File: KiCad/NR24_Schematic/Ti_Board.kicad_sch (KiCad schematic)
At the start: 25 parts, among them J5 Dash TI Connection, J5 J1 Pin J3 Pin, J5 J12 (CAN Interface w/ Transce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, J5 J4 Pin J2 Pin, J5 J5 Pin J7 Pin, J5 J8 Pin J6 Pin, J5 XBEE PRO, J6 SpeakON_NL2, J8 CAN Connector, Q1 Q_NMOS_DGS, Q2 Q_NMOS_DGS, Q3 Q_NMOS_DGS

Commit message: NOV1 Changes w Clarks
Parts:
- added J5: J4 Pin J2 Pin, symbol Connector_Generic:Conn_02x06_Counter_Clockwise
- added J5: J1 Pin J3 Pin, symbol Connector_Generic:Conn_02x06_Counter_Clockwise

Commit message: ams with IMD inside
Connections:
- net in_BLK: now also Q1.1 (D), Q2.1 (D); no longer Q1.2 (G), Q2.2 (G)
- net at R3.2: now also Q1.2 (G); no longer Q1.1 (D)
- net Yellow to RCKR Switch: now reaches J5.1 (3.3V)
- net White to CANBUS Plug: now reaches J5.21 (5V)
- net at R4.2: now also Q2.2 (G); no longer Q2.1 (D)
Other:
- moved on the sheet: R3, R4

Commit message: stuff
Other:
- note added: "Old NR23 Dash"
- moved on the sheet: D2, D3, J6, Q1, Q2, Q3, R1, R2, R3, R4

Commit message: AMS with relay
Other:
- note removed: "Old NR23 Dash"
- moved on the sheet: D2, D3, J6, Q1, Q2, Q3, R1, R2, R3, R4

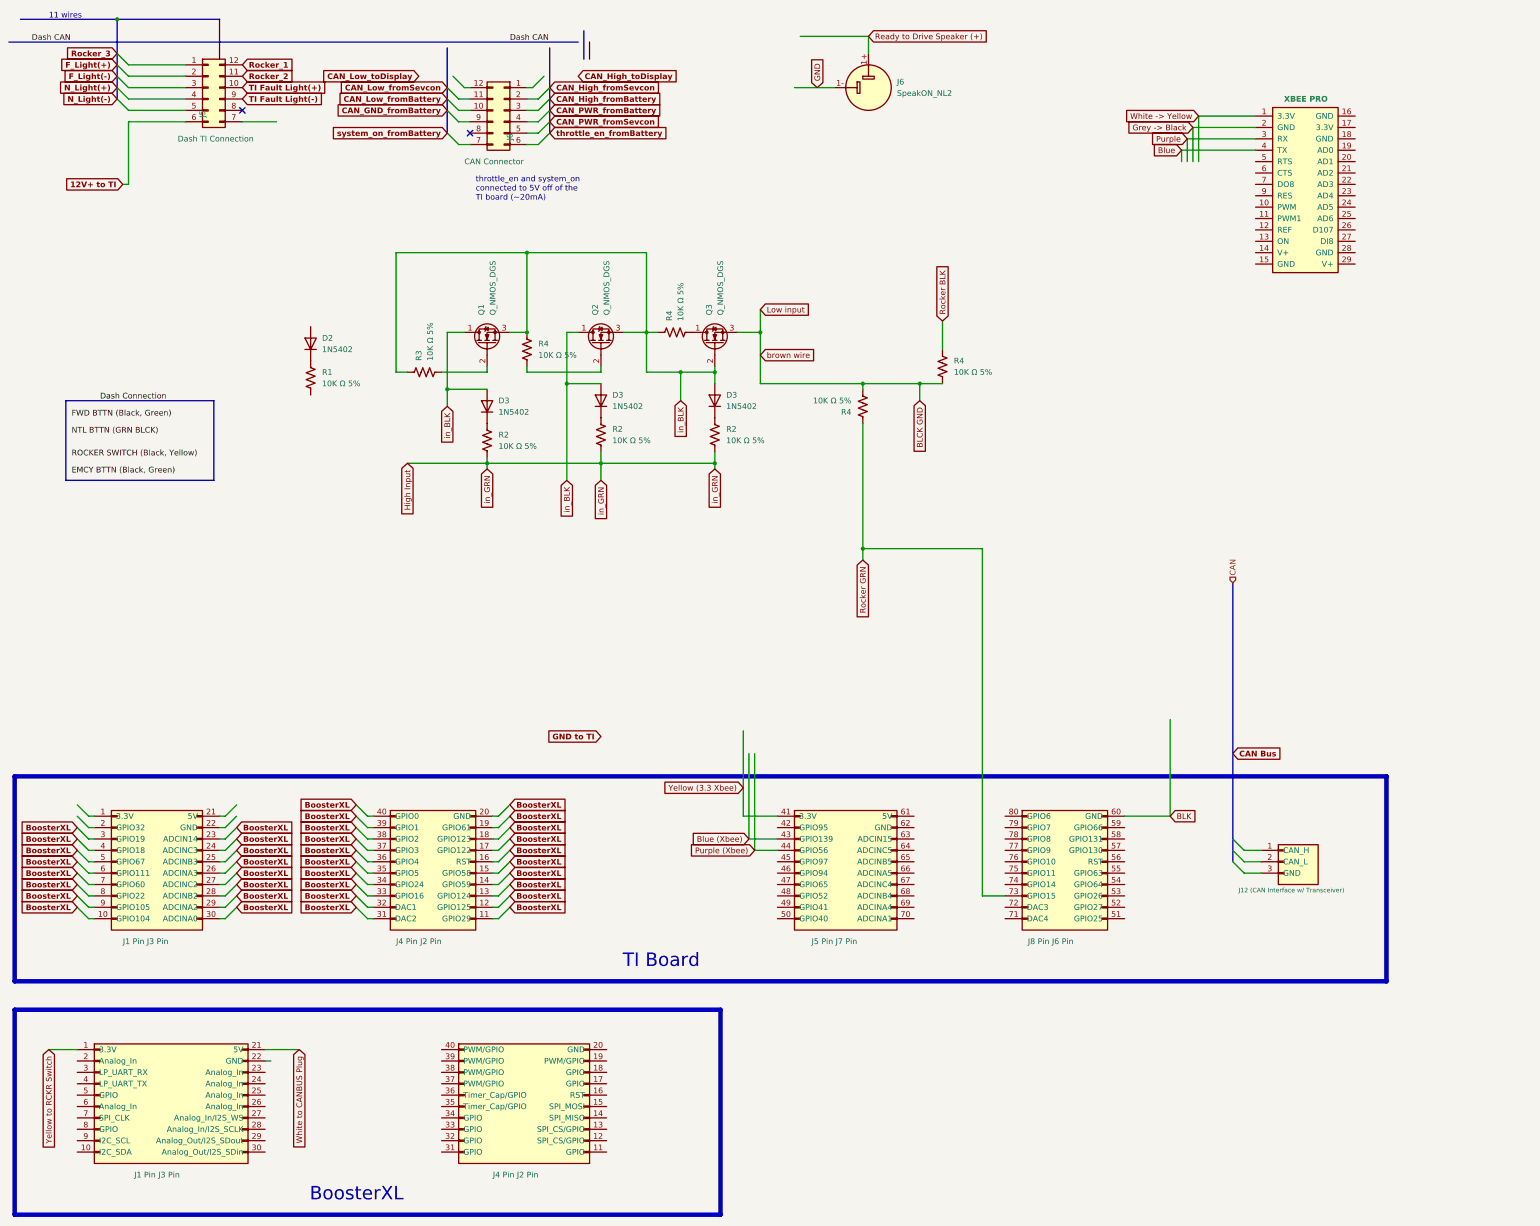
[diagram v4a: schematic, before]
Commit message: Update Ti_Board.kicad_sch
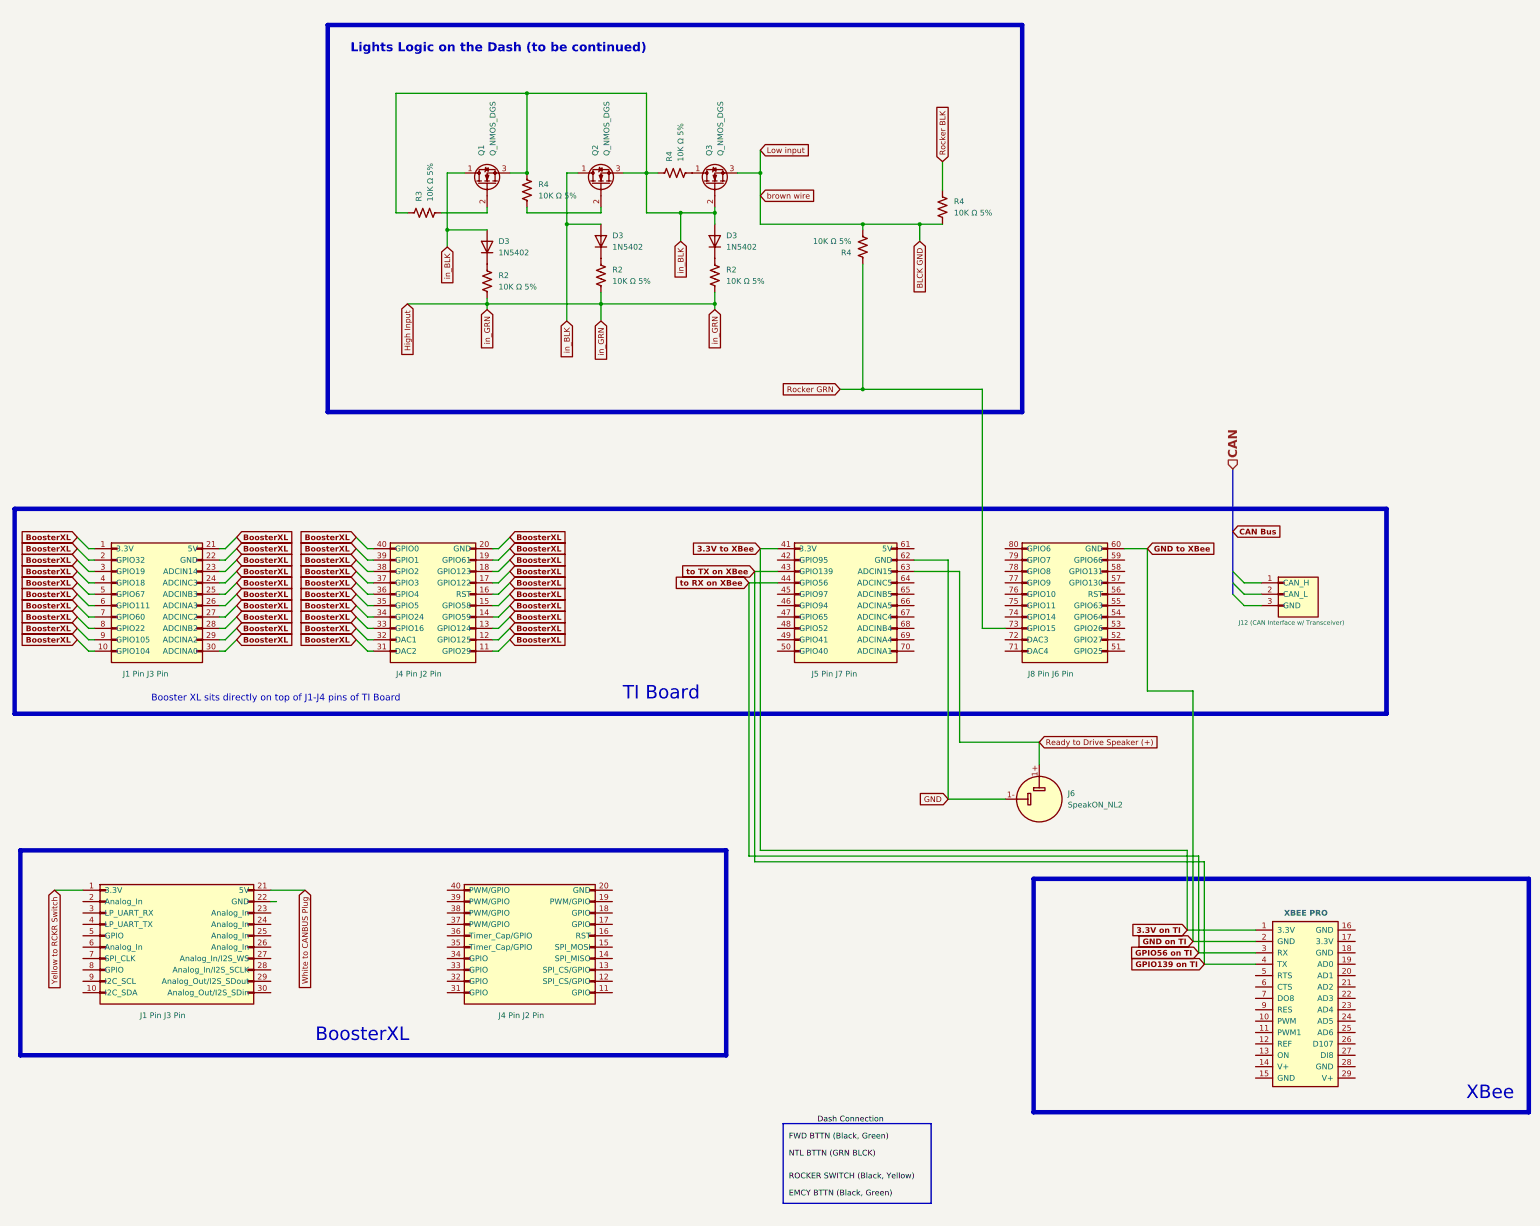
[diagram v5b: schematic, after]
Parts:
- removed D2: 1N5402, Diode_THT:D_DO-201AD_P15.24mm_Horizontal, symbol Diode:1N5402
- removed J5: Dash TI Connection, symbol Connector_Generic:Conn_02x06_Counter_Clockwise
- removed J8: CAN Connector, symbol Connector_Generic:Conn_02x06_Counter_Clockwise
- removed R1: 10K Ω 5%, symbol Device:R_US
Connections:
- net Blue (Xbee) is gone; now on net GPIO139 on TI: J5.43 (GPIO139)
- net Grey -> Black is gone; now on net GND on TI: J5.2 (GND)
- net Purple (Xbee) is gone; now on net GPIO56 on TI: J5.44 (GPIO56)
- net Yellow (3.3 Xbee) is gone; now on net 3.3V on TI: J5.41 (3.3V)
- net GND: now also J5.62 (GND)
- net Ready to Drive Speaker (+): now also J5.63 (ADCIN15)
- net BLK renamed GND on TI
- net Blue renamed GPIO139 on TI
- net Purple renamed GPIO56 on TI
- net White -> Yellow renamed 3.3V on TI
- no-connect marks 2 -> 0
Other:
- note added: "Booster XL sits directly on top of J1-J4 pins of TI Board"
- note added: "Lights Logic on the Dash (to be continued)"
- note added: "XBee"
- note removed: "11 wires"
- note removed: "throttle_en and system_on connected to 5V off of the TI board (~20mA)"
- moved on the sheet: D3, J6, Q1, Q2, Q3, R2, R3, R4

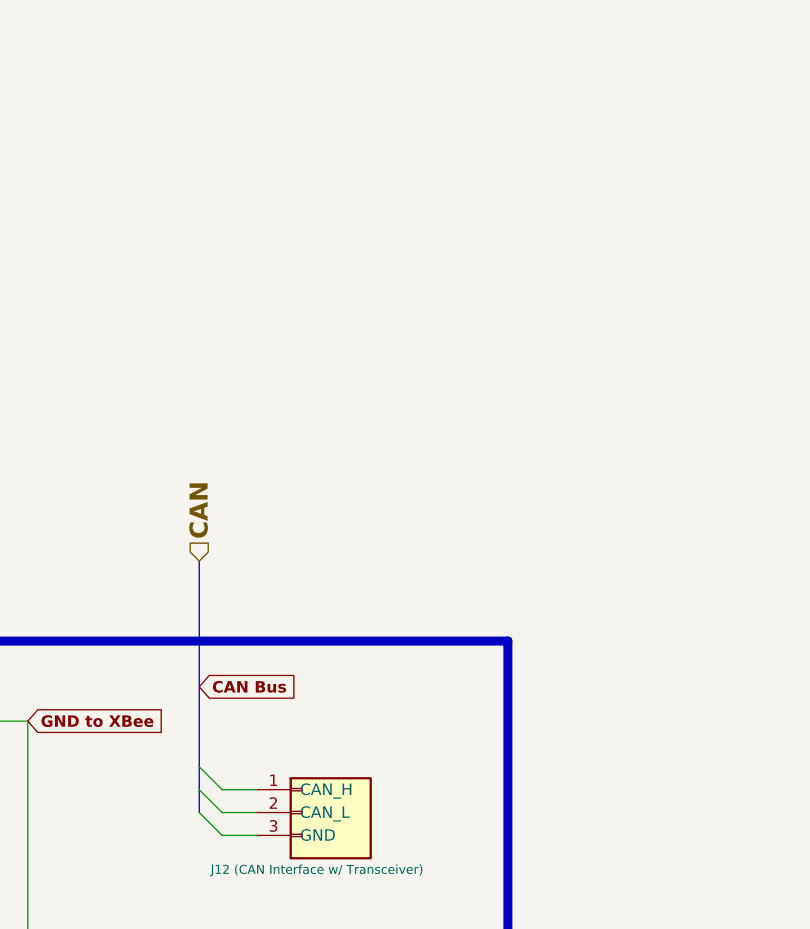
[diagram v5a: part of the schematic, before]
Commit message: Update Ti_Board.kicad_sch
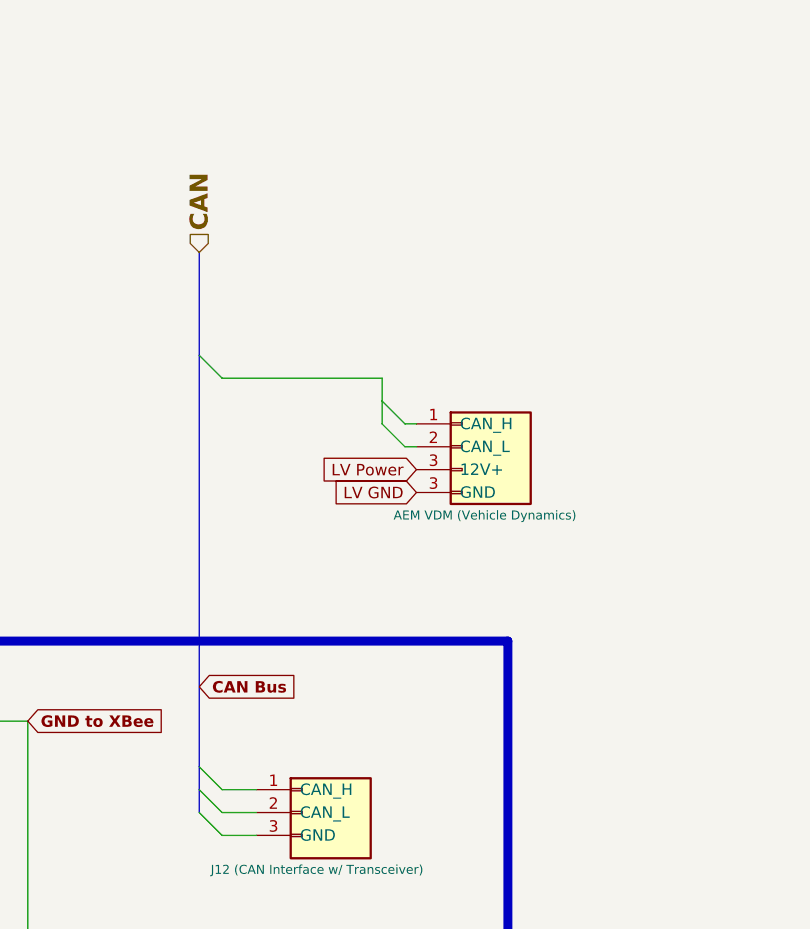
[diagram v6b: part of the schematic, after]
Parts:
- added J5: AEM VDM (Vehicle Dynamics), symbol Connector_Generic:Conn_02x06_Counter_Clockwise
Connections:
- new net LV GND: J5.3 (GND)
- new net LV Power: J5.3 (GND)
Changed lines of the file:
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@@
     (stroke (width 0) (type default))
+  )
+  (bus_entry (at 308.61 99.06) (size 2.54 2.54)
+    (stroke (width 0.75) (type default) (color 0 132 132 1))
   )
   (bus_entry (at 66.04 149.86) (size -2.54 2.54)
@@
     (stroke (width 0) (type default))
   )
+  (bus_entry (at 288.29 93.98) (size 2.54 2.54)
+    (stroke (width 0.75) (type default) (color 0 132 132 1))
+  )
   (bus_entry (at 127 132.08) (size -2.54 2.54)
     (stroke (width 0) (type default))
   )
+  (bus_entry (at 308.61 101.6) (size 2.54 2.54)
+    (stroke (width 0.75) (type default) (color 0 132 132 1))
+  )
   (bus_entry (at 92.71 142.24) (size 2.54 2.54)
     (stroke (width 0) (type default))
@@
   (wire (pts (xy 280.67 203.2) (xy 180.34 203.2))
     (stroke (width 0) (type default))
+  )
+  (wire (pts (xy 290.83 96.52) (xy 308.61 96.52))
+    (stroke (width 0.75) (type default) (color 0 132 132 1))
   )
   (wire (pts (xy 33.02 134.62) (xy 34.29 134.62))
@@
     (stroke (width 0) (type default))
   )
+  (wire (pts (xy 308.61 99.06) (xy 308.61 101.6))
+    (stroke (width 0.75) (type default) (color 0 132 132 1))
+  )
   (wire (pts (xy 33.02 142.24) (xy 34.29 142.24))
     (stroke (width 0) (type default))
@@
     (stroke (width 0) (type default))
   )
+  (wire (pts (xy 308.61 99.06) (xy 308.61 96.52))
+    (stroke (width 0.75) (type default) (color 0 132 132 1))
+  )
   (wire (pts (xy 123.19 144.78) (xy 124.46 144.78))
     (stroke (width 0) (type default))
@@
     (stroke (width 0) (type default))
   )
-  (bus (pts (xy 288.29 116.84) (xy 288.29 139.7))
+  (bus (pts (xy 288.29 82.55) (xy 288.29 93.98))
     (stroke (width 0.75) (type default) (color 0 132 132 1))
   )
@@
     (stroke (width 0) (type default))
   )
+  (bus (pts (xy 288.29 93.98) (xy 288.29 139.7))
+    (stroke (width 0.75) (type default) (color 0 132 132 1))
+  )
   (wire (pts (xy 121.92 80.01) (xy 147.32 80.01))
     (stroke (width 0) (type default))
@@
     (stroke (width 0) (type default))
   )
+  (wire (pts (xy 311.15 101.6) (xy 312.42 101.6))
+    (stroke (width 0) (type default))
+  )
   (wire (pts (xy 95.25 154.94) (xy 96.52 154.94))
     (stroke (width 0) (type default))
@@
   )
   (wire (pts (xy 95.25 144.78) (xy 96.52 144.78))
+    (stroke (width 0) (type default))
+  )
+  (wire (pts (xy 311.15 104.14) (xy 312.42 104.14))
     (stroke (width 0) (type default))
   )
@@
     )
   )
+  (global_label "LV Power" (shape input) (at 312.42 106.68 180) (fields_autoplaced)
+    (effects (font (size 1.27 1.27)) (justify right))
+    (property "Intersheetrefs" "${INTERSHEET_REFS}" (at 300.7262 106.68 0)
+      (effects (font (size 1.27 1.27)) (justify right) hide)
+    )
+  )
   (global_label "BoosterXL" (shape input) (at 127 144.78 0) (fields_autoplaced)
     (effects (font (size 1.27 1.27) (thickness 0.254) bold) (justify left))
@@
     )
   )
+  (global_label "LV GND" (shape input) (at 312.42 109.22 180) (fields_autoplaced)
+    (effects (font (size 1.27 1.27)) (justify right))
+    (property "Intersheetrefs" "${INTERSHEET_REFS}" (at 302.48 109.22 0)
+      (effects (font (size 1.27 1.27)) (justify right) hide)
+    )
+  )
   (global_label "BoosterXL" (shape input) (at 92.71 134.62 180) (fields_autoplaced)
     (effects (font (size 1.27 1.27) (thickness 0.254) bold) (justify right))
@@
     )
   )
-  (hierarchical_label "CAN" (shape input) (at 288.29 116.84 90) (fields_autoplaced)
+  (hierarchical_label "CAN" (shape input) (at 288.29 82.55 90) (fields_autoplaced)
     (effects (font (size 2 2) (thickness 0.4) bold (color 0 194 194 1)) (justify left))
   )
@@
         )
       )
+    )
+  )
+  (symbol (lib_name "Conn_02x06_Counter_Clockwise_9") (lib_id "Connector_Generic:Conn_02x06_Counter_Clockwise") (at 327.66 107.95 0) (unit 1)
+    (in_bom yes) (on_board yes) (dnp no)
+    (property "Reference" "J5" (at 313.69 119.38 90)
+      (effects (font (size 1.27 1.27)) (justify right) hide)
+    )
+    (property "Value" "AEM VDM (Vehicle Dynamics)" (at 309.88 111.76 0)
+      (effects (font (size 1 1)) (justify left))
+    )
+    (property "Footprint" "" (at 317.5 106.68 0)
+      (effects (font (size 1.27 1.27)) hide)
+    )
+    (property "Datasheet" "~" (at 317.5 107.95 0)
+      (effects (font (size 1.27 1.27)) hide)
+    )
+    (pin "1")
+    (pin "2")
+    (pin "3")
+    (pin "3")
+    (instances
+      (project "Car_TractiveSystem_v2"
+        (path "/588b5c14-1813-4e1d-9dbe-940839ecebe3"
+          (reference "J5") (unit 1)
+        )
+        (path "/588b5c14-1813-4e1d-9dbe-940839ecebe3/42103732-fa28-467e-b394-54af70cbf903"
+          (reference "J3") (unit 1)
+        )
+      )
+      (project "Ti_Board"
+        (path "/95cd4c17-85c0-46ed-9908-1b2dc6d240f0"
+          (reference "J4") (unit 1)
+        )
+      )
